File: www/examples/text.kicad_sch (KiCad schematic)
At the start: 0 parts

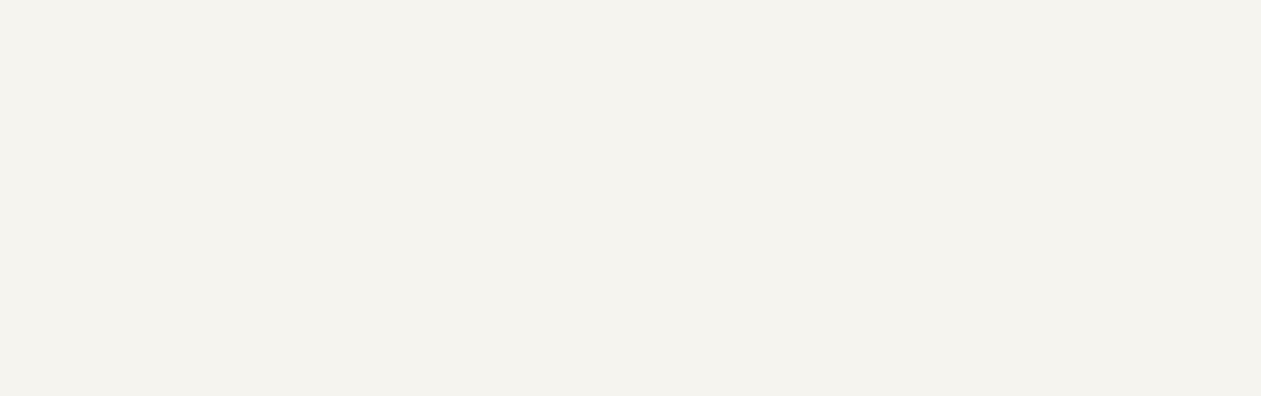
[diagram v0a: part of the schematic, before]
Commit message: Add examples of custom fonts in text examples
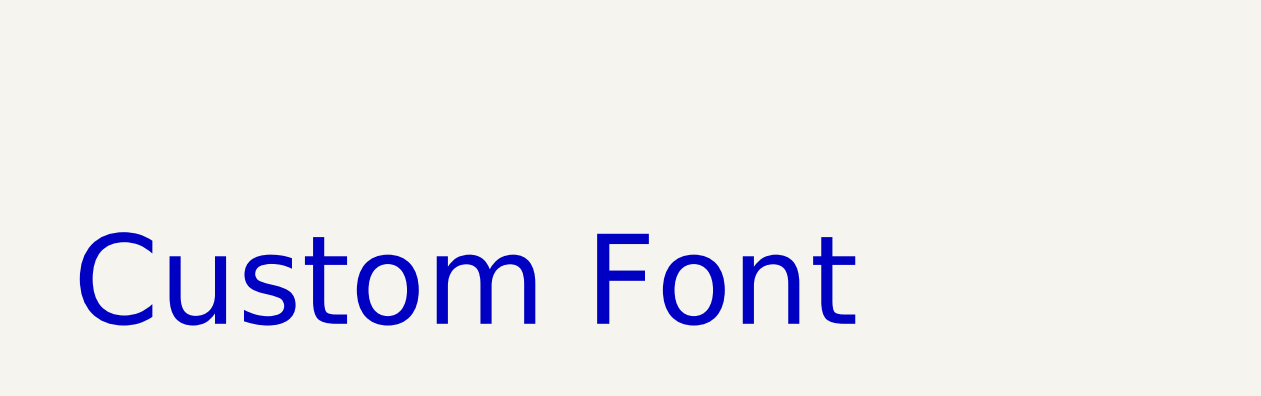
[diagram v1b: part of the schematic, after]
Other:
- note added: "Custom Font"
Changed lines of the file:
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@@
     (effects (font (size 2.54 2.54) (thickness 0.254) bold) (justify left bottom))
+  )
+  (text "Custom Font" (at 13.97 195.58 0)
+    (effects (font (face "Pluto") (size 10 10)) (justify left bottom))
   )
   (text "BOLD & ITALIC BOTTOM 1.27" (at 134.62 76.2 90)
